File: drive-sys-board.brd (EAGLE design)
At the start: 109.9 x 50.2 mm, 32 parts, among them J2 APP_2POS_CONFIG12V_HORIZ, U1 OKI-78SR-5/1.5-W36HC, U2 MAX232D, U3 MAX232D, U4 MAX232D

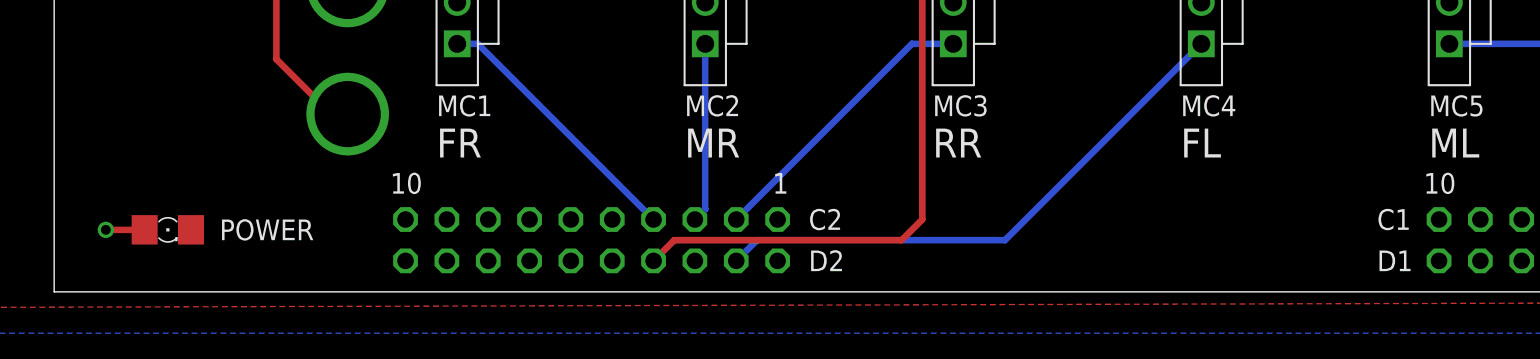
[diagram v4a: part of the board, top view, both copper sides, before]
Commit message: Prep for Board Review
- Labeled schematic with corresponding Serial channels (from hardware
serial on Tiva.
- Added Power Indicator LED and Debug LED
- Still need to decide on current limiting resistors for LEDs
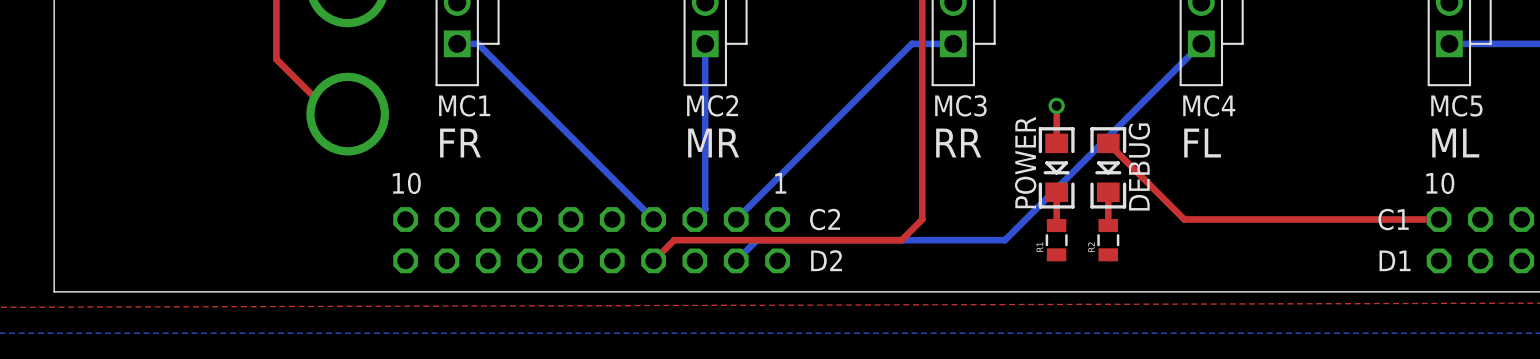
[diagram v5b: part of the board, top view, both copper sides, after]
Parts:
- added DEBUG: RED, SparkFun-LED:LED-1206
- added R1, R2: ?, SparkFun-Resistors:0805
- POWER: value (none) -> GREEN; device eagle-ltspice:LED_1206 -> SparkFun-LED:LED-1206
- moved POWER 54.7 mm to (61.6, 7.62), turned to 270 degrees
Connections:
- new net DEBUG: DEBUG.A, U$1.PL3
- new net N$10: DEBUG.C, R2.2
- new net N$17: POWER.C, R1.2
- net +5V: now also R1.1, R2.1; no longer POWER.C
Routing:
- net DEBUG: track 0.00 -> 22.3 mm
- net N$17: track 0.00 -> 2.04 mm
- net N$10: track 0.00 -> 2.04 mm
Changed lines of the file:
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@@
 <?xml version="1.0" encoding="utf-8"?>
 <!DOCTYPE eagle SYSTEM "eagle.dtd">
-<eagle version="7.6.0">
+<eagle version="7.7.0">
 <drawing>
 <settings>
@@
 <attribute name="VALUE" x="13.716" y="29.972" size="0.4064" layer="27" rot="R180"/>
 </element>
-<element name="POWER" library="eagle-ltspice" package="LED_1206" value="" x="6.985" y="3.81" smashed="yes">
-<attribute name="SPICETYPE" value="diode" x="6.985" y="3.81" size="1.778" layer="27" display="off"/>
-<attribute name="SPICEPREFIX" value="D" x="6.985" y="3.81" size="1.778" layer="27" display="off"/>
-<attribute name="SPICEMODEL" value="NONE" x="6.985" y="3.81" size="1.778" layer="27" display="off"/>
-<attribute name="NAME" x="10.16" y="3.175" size="1.27" layer="25"/>
-<attribute name="VALUE" x="5.715" y="1.27" size="1.27" layer="27"/>
+<element name="POWER" library="SparkFun-LED" package="LED-1206" value="GREEN" x="61.595" y="7.62" smashed="yes" rot="R270">
+<attribute name="PROD_ID" value="DIO-00862" x="61.595" y="7.62" size="1.778" layer="27" rot="R270" display="off"/>
+<attribute name="NAME" x="59.055" y="10.795" size="1.27" layer="25" rot="R270"/>
+<attribute name="VALUE" x="59.817" y="8.636" size="0.4064" layer="27" rot="R270"/>
+</element>
+<element name="DEBUG" library="SparkFun-LED" package="LED-1206" value="RED" x="64.77" y="7.62" smashed="yes" rot="R270">
+<attribute name="PROD_ID" value="DIO-09912" x="64.77" y="7.62" size="1.778" layer="27" rot="R270" display="off"/>
+<attribute name="NAME" x="66.04" y="10.4775" size="1.27" layer="25" rot="R270"/>
+<attribute name="VALUE" x="62.992" y="8.636" size="0.4064" layer="27" rot="R270"/>
+</element>
+<element name="R1" library="SparkFun-Resistors" package="0805" value="?" x="61.595" y="3.175" rot="R90">
+<attribute name="PROD_ID" value="RES-09883" x="61.595" y="3.175" size="1.27" layer="27" rot="R90" display="off"/>
+</element>
+<element name="R2" library="SparkFun-Resistors" package="0805" value="?" x="64.77" y="3.175" rot="R90">
+<attribute name="PROD_ID" value="RES-09883" x="64.77" y="3.175" size="1.27" layer="27" rot="R90" display="off"/>
 </element>
 </elements>
@@
 <wire x1="10.922" y1="30.607" x2="10.922" y2="31.1785" width="0.4064" layer="1"/>
 <contactref element="POWER" pad="A"/>
-<via x="3.175" y="3.81" extent="1-16" drill="0.6" shape="square"/>
-<wire x1="5.563" y1="3.81" x2="3.175" y2="3.81" width="0.4064" layer="1"/>
+<via x="61.595" y="11.43" extent="1-16" drill="0.6" shape="square"/>
+<wire x1="61.595" y1="9.12" x2="61.595" y2="11.43" width="0.4064" layer="1"/>
 </signal>
 <signal name="+5V">
@@
 <contactref element="C5_2" pad="2"/>
 <contactref element="C5_3" pad="2"/>
-<contactref element="POWER" pad="C"/>
+<contactref element="R1" pad="1"/>
+<contactref element="R2" pad="1"/>
 </signal>
 <signal name="PWM_6">
@@
 <wire x1="35.93" y1="31.38" x2="36.195" y2="31.38" width="0.4064" layer="1"/>
 </signal>
+<signal name="DEBUG">
+<contactref element="U$1" pad="PL3"/>
+<contactref element="DEBUG" pad="A"/>
+<wire x1="85.09" y1="4.445" x2="69.445" y2="4.445" width="0.4064" layer="1"/>
+<wire x1="69.445" y1="4.445" x2="64.77" y2="9.12" width="0.4064" layer="1"/>
+</signal>
+<signal name="N$10">
+<contactref element="DEBUG" pad="C"/>
+<contactref element="R2" pad="2"/>
+<wire x1="64.77" y1="6.12" x2="64.77" y2="4.075" width="0.4064" layer="1"/>
+</signal>
+<signal name="N$17">
+<contactref element="POWER" pad="C"/>
+<contactref element="R1" pad="2"/>
+<wire x1="61.595" y1="6.12" x2="61.595" y2="4.075" width="0.4064" layer="1"/>
+</signal>
 </signals>

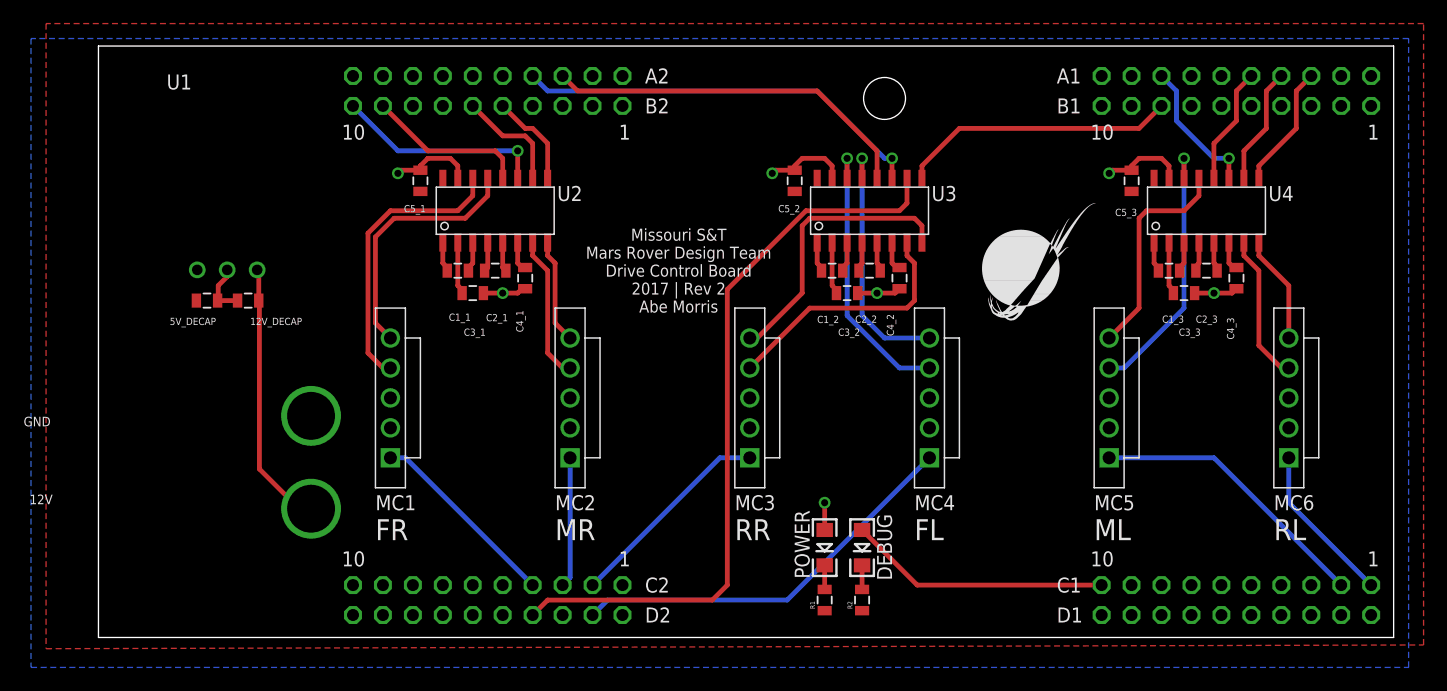
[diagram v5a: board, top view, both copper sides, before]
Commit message: Adjusted labels and removed top +5V plane
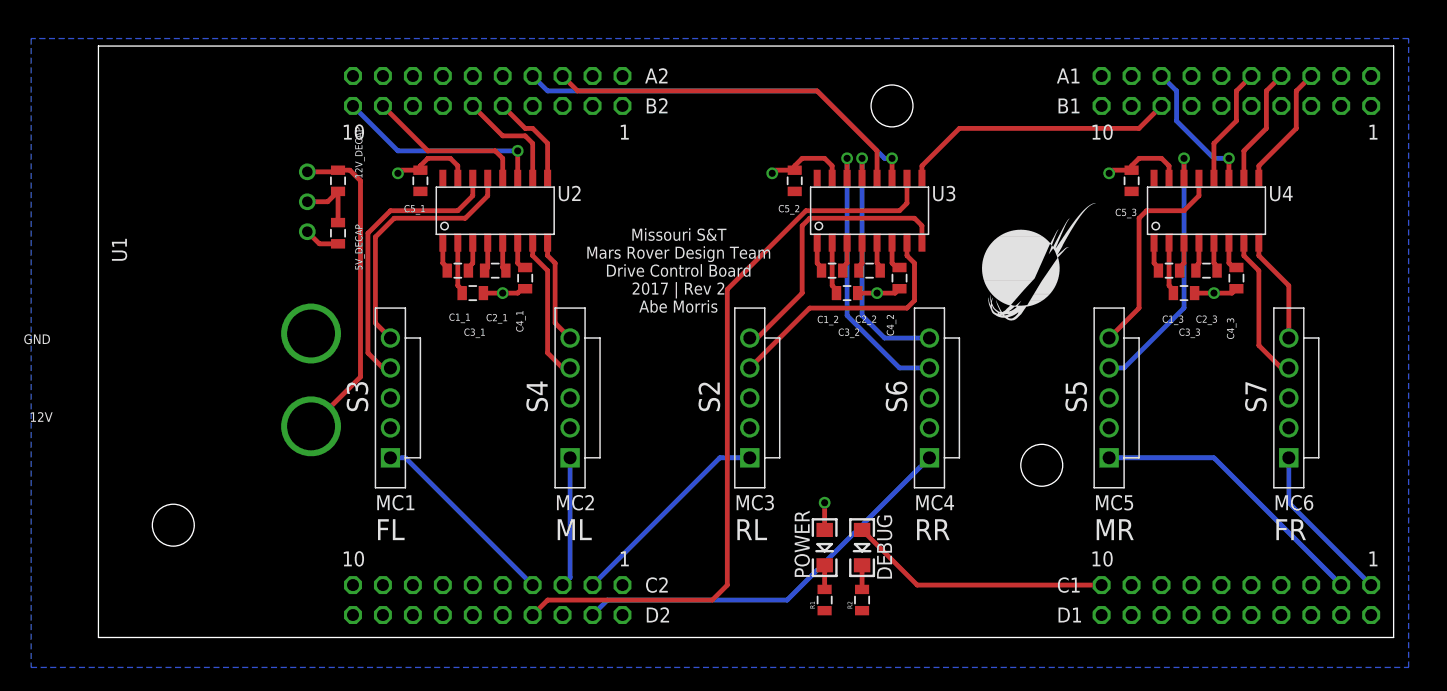
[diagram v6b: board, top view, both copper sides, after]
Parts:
- added H1, H3: MOUNTING_HOLE#6, MRDT-Hardware:#6_SCREW
- R1, R2: value ? -> 330
- moved 12V_DECAP 12.7 mm to (20.3, 38.7), turned to 270 degrees
- moved 5V_DECAP 12.5 mm to (20.3, 34.3), turned to 270 degrees
- moved U1 9.34 mm to (17.7, 39.5), turned to 90 degrees
- moved J2 6.99 mm to (-10.2, 14.0)
- moved H2 0.90 mm to (67.3, 45.1)
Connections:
- net +5V: no longer MC1.2, MC2.2, MC3.2, MC4.2, MC5.2, MC6.2
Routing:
- net N$5: track 22.7 -> 27.5 mm
- net +5V: track 0.00 -> 3.03 mm
- net GND: track 39.6 -> 40.6 mm
- removed copper zone on layer 1, net +5V
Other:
- board text added: "S2"
- board text added: "S3"
- board text added: "S4"
- board text added: "S5"
- board text added: "S6"
- board text added: "S7"

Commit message: Rerouted RS232 Connections
Moved RS232 ICs down slightly and rerouted to avoid the +5V trace.
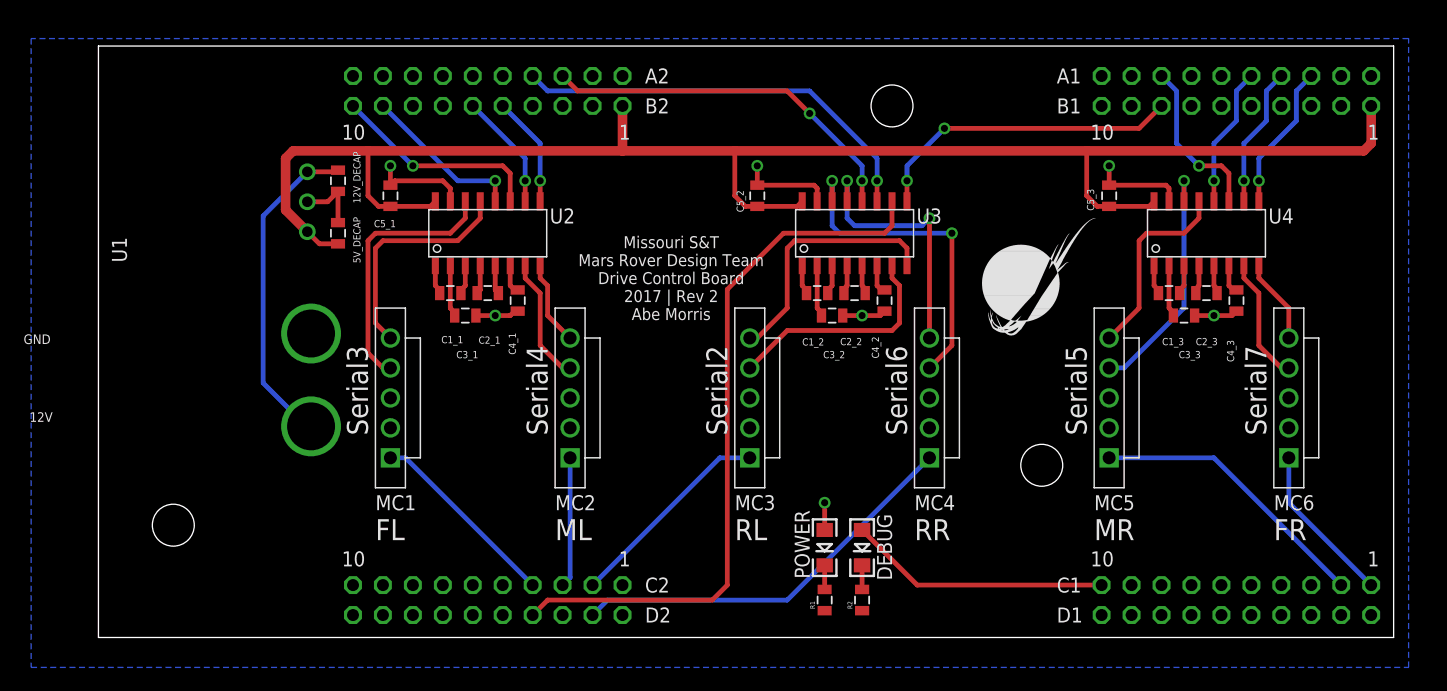
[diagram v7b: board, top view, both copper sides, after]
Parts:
- moved C5_2 3.42 mm to (55.9, 37.5)
- moved C5_1 2.84 mm to (24.8, 37.5)
- moved C3_2 2.29 mm to (62.2, 27.3)
- moved C4_2 2.29 mm to (66.7, 28.6)
- moved C5_3 2.29 mm to (85.7, 37.5)
- moved U3 2.29 mm to (64.1, 34.3)
- moved C1_2 2.29 mm to (61.0, 29.2)
- moved C2_2 2.29 mm to (64.1, 29.2)
- moved C3_1 2.01 mm to (31.1, 27.3)
- moved C4_1 2.01 mm to (35.6, 28.6)
- moved U2 2.01 mm to (33.0, 34.3)
- moved C1_1 2.01 mm to (29.8, 29.2)
- moved C2_1 2.01 mm to (33.0, 29.2)
- moved C3_3 1.91 mm to (92.1, 27.3)
- moved C4_3 1.91 mm to (96.5, 28.6)
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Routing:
- net +5V: track 3.03 -> 139.8 mm
- net N$32: track 23.9 -> 28.2 mm, vias 1 -> 2
- net RX_4: track 23.5 -> 26.7 mm, vias 0 -> 2
- net GND: track 40.6 -> 43.1 mm
- net N$30: track 23.9 -> 21.4 mm
- net TX_5: track 11.8 -> 14.1 mm
- net N$31: track 21.5 -> 19.5 mm
- net TX_4: track 63.0 -> 60.9 mm
- net N$37: track 21.5 -> 19.5 mm
- net TX_6: track 10.0 -> 12.0 mm, vias 0 -> 1
- net RX_6: track 10.6 -> 12.5 mm, vias 0 -> 1
- net RX_5: track 10.0 -> 12.0 mm, vias 0 -> 1
- net N$29: track 18.5 -> 16.6 mm
- net N$26: track 22.9 -> 21.0 mm
- net N$28: track 12.6 -> 10.7 mm
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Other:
- board text added: "Serial2"
- board text added: "Serial3"
- board text added: "Serial4"
- board text added: "Serial5"
- board text added: "Serial6"
- board text added: "Serial7"
- board text removed: "S2"
- board text removed: "S3"
- board text removed: "S4"
- board text removed: "S5"
- board text removed: "S6"
- board text removed: "S7"

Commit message: Finished routing
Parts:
- moved U$2 68.0 mm to (10.8, 2.25)
- moved R1 6.38 mm to (61.0, 9.53), turned to 270 degrees
- moved R2 6.35 mm to (64.8, 9.53), turned to 270 degrees
- moved POWER 2.62 mm to (61.0, 5.08), turned to 90 degrees
- moved DEBUG 2.54 mm to (64.8, 5.08), turned to 90 degrees
- moved C4_1 2.54 mm to (35.6, 26.0), turned to 0 degrees
- moved C4_2 2.54 mm to (66.7, 26.0), turned to 0 degrees
- moved C4_3 2.54 mm to (96.5, 26.0), turned to 0 degrees
- moved C1_3 1.42 mm to (89.5, 28.6), turned to 90 degrees
- moved C1_2 1.42 mm to (59.7, 28.6), turned to 90 degrees
- moved C3_3 1.42 mm to (91.4, 26.0)
- moved C1_1 1.42 mm to (28.6, 28.6), turned to 90 degrees
- moved C3_1 1.42 mm to (30.5, 26.0)
- moved C3_2 1.42 mm to (61.6, 26.0)
- moved C2_1 0.64 mm to (33.0, 28.6)
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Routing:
- net +5V: track 139.8 -> 178.1 mm, vias 0 -> 2
- net N$21: track 4.44 -> 12.1 mm
- net N$14: track 4.44 -> 12.1 mm
- net N$8: track 4.44 -> 12.1 mm
- net N$15: track 2.53 -> 6.19 mm
- net N$22: track 2.53 -> 6.19 mm
- net N$9: track 2.53 -> 6.19 mm
- net N$19: track 2.53 -> 5.56 mm
- net N$4: track 2.53 -> 5.56 mm
- net N$12: track 2.53 -> 5.56 mm
- net N$31: track 19.5 -> 21.8 mm
- net N$37: track 19.5 -> 17.7 mm
- net DEBUG: track 22.3 -> 20.7 mm
- net GND: track 43.1 -> 41.7 mm
- net N$29: track 16.6 -> 18.1 mm
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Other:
- outline, holes or cut-outs redrawn
